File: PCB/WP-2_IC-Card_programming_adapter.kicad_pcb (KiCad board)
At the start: 2 copper layers, 17.8 x 49.5 mm, 4 parts, among them J1 Conn_01x38_Male, J2 Conn_02x16_Counter_Clockwise, J3 Conn_02x08_Odd_Even

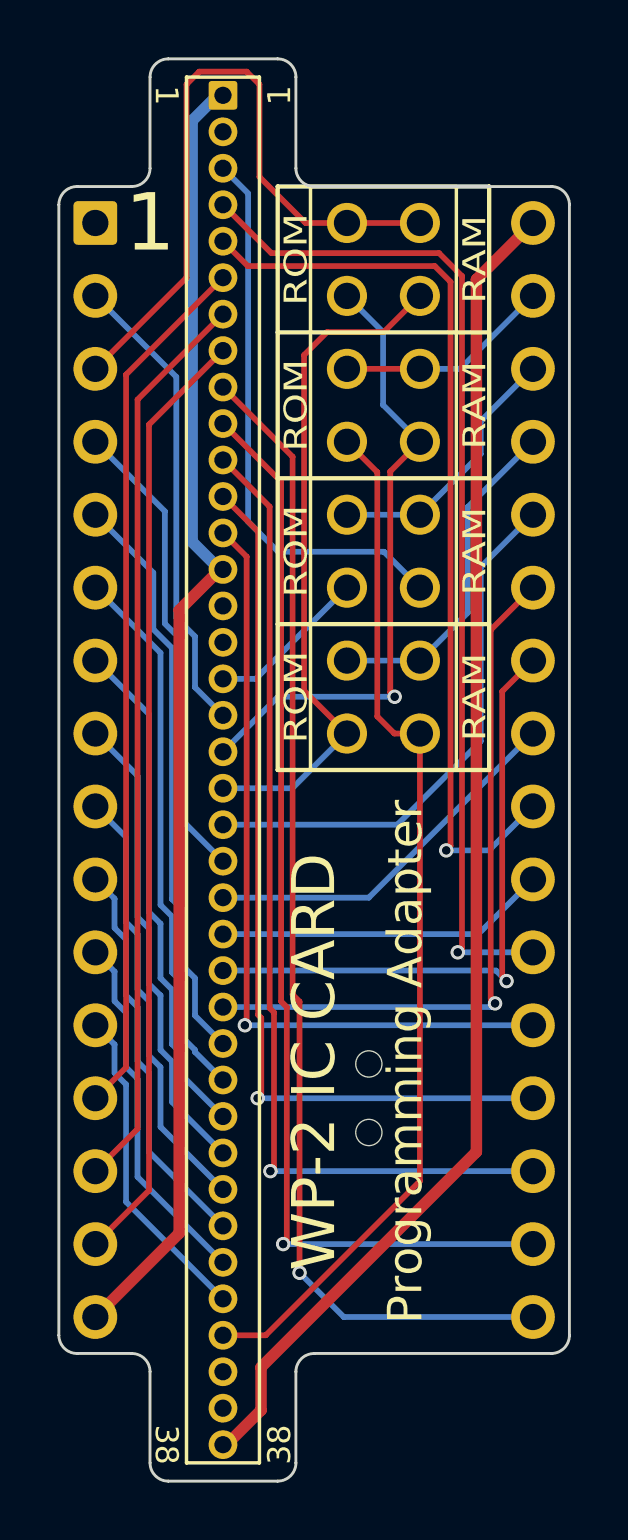
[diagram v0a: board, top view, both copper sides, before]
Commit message: MRAM level shifters, delete FRAM, local datasheets in local symbols
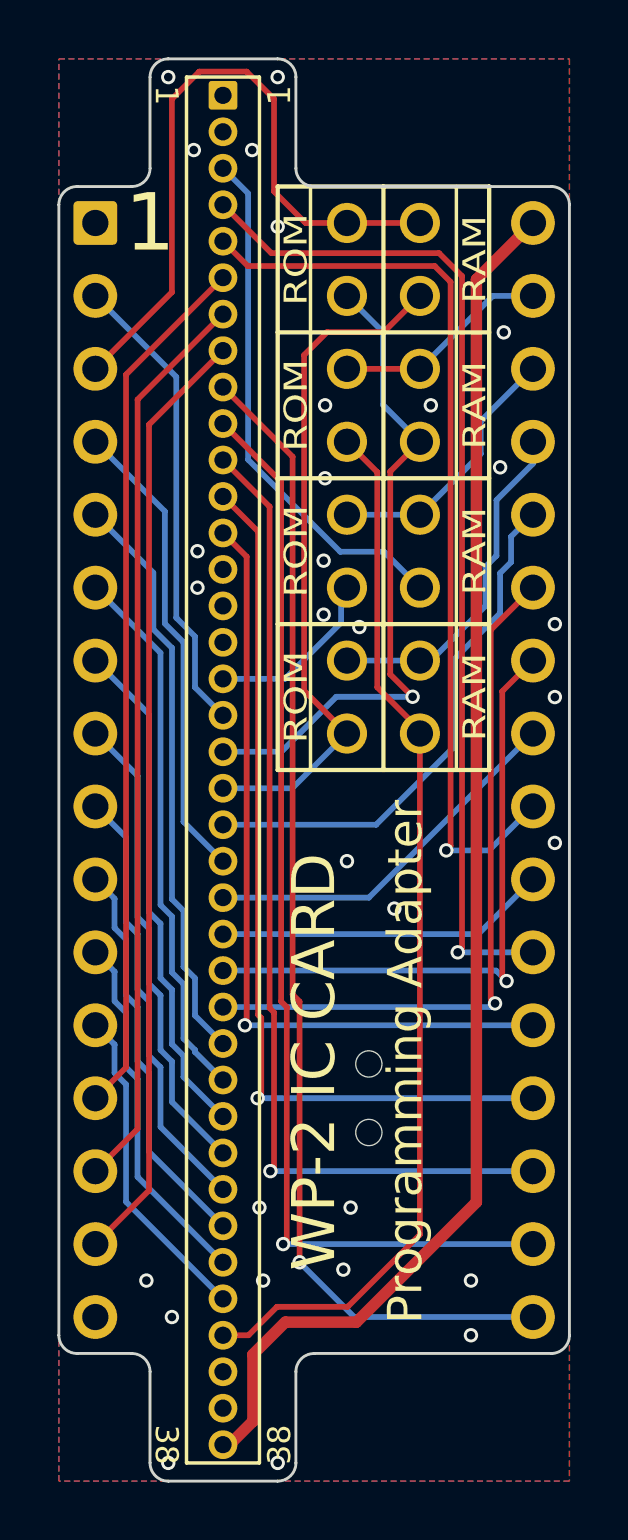
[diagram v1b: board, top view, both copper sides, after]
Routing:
- net GND: track 45.5 -> 0.40 mm, vias 0 -> 30
- net VDD: track 47.1 -> 48.6 mm
- net /CE2: track 19.6 -> 18.3 mm
- net /A15: track 22.3 -> 23.2 mm
- net /A17: track 5.63 -> 6.23 mm
- net /R~{W}: track 36.4 -> 37.0 mm
- added copper zone on B.Cu, net GND
- added copper zone on F.Cu, net GND

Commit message: local symbol & footprint library organization, add shielded mram version
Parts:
- J1: footprint 0_LOCAL:Pin_Header_Straight_1x38_Pitch1.27mm -> 000_LOCAL:Pin_Header_Straight_1x38_Pitch1.27mm
- J2: footprint 0_LOCAL:2x16x600 -> 000_LOCAL:2x16x600
- J3: footprint 0_LOCAL:2x8_jumper_block -> 000_LOCAL:2x8_jumper_block
- REF**: footprint 0_LOCAL:JP2_tight_storage -> 000_LOCAL:JP2_tight_storage

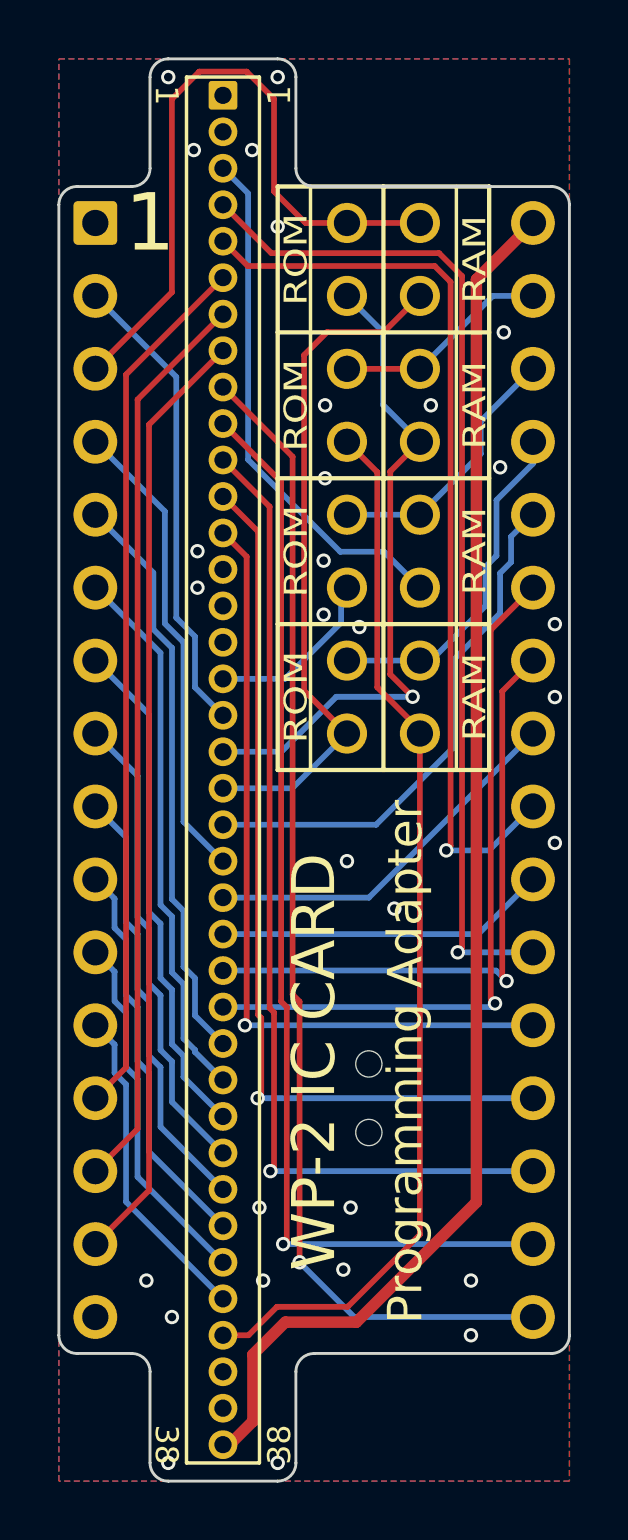
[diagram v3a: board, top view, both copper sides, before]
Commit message: update programming adapter & readme
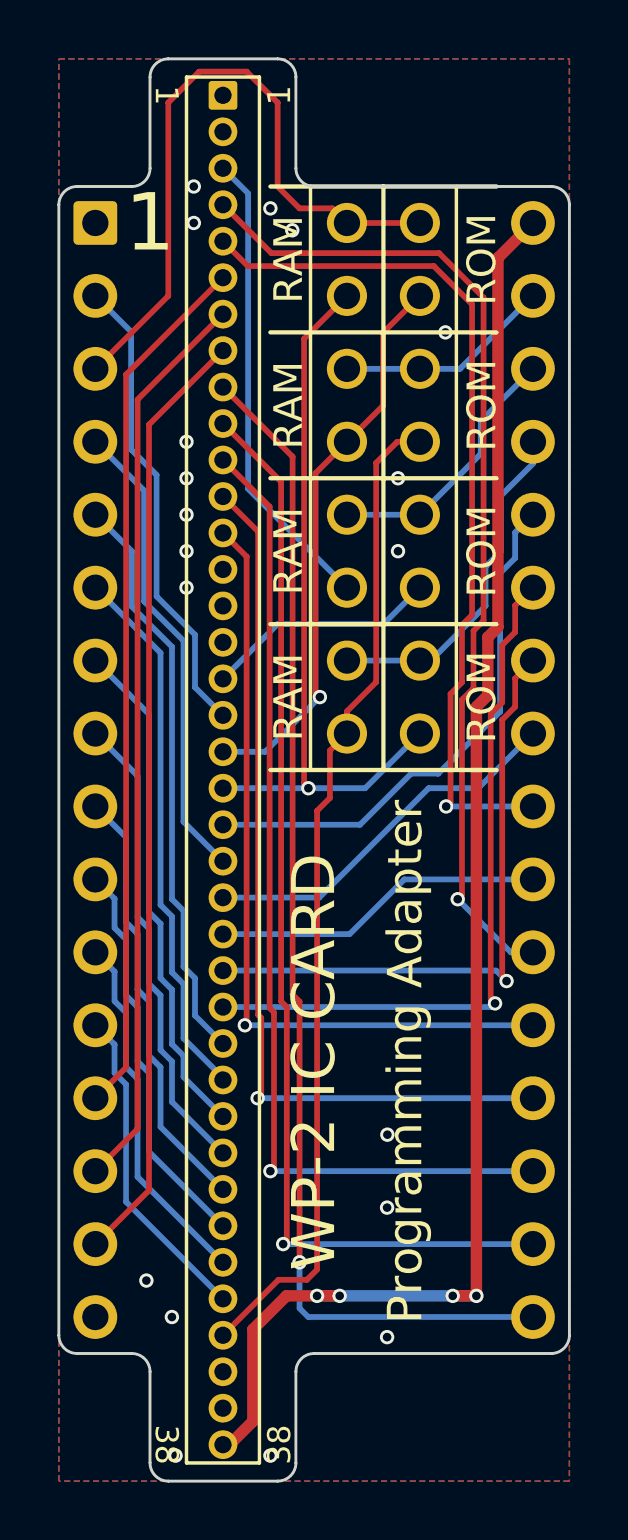
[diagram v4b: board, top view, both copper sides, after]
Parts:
- removed REF**: , 000_LOCAL:JP2_tight_storage
- J2: value Conn_02x16_Counter_Clockwise -> SST39SF020_DIP
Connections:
- net VDD renamed VCC
- J1 pad 14: GND -> /T2
- J1 pad 15: (no net) -> /S1
- J1 pad 16: (no net) -> /S2
- J1 pad 2: (no net) -> /~{DET}
- J1 pad 36: (no net) -> /S3
- J1 pad 37: (no net) -> /BCHK
- J2 pad 1: (no net) -> unconnected-(J2-NC-Pad1)
- J3 pad 11: /A17 -> /CE2
- J3 pad 12: /CE2 -> /A17
- J3 pad 15: /A14 -> /R~{W}
- J3 pad 16: /R~{W} -> /A14
- J3 pad 3: /A15 -> /A14
- J3 pad 4: /A14 -> /A15
- J3 pad 7: /R~{W} -> /A15
- J3 pad 8: /A15 -> /R~{W}
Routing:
- net VCC: track 48.6 -> 52.6 mm, vias 0 -> 4
- net /A15: track 23.2 -> 19.7 mm
- net /R~{W}: track 37.0 -> 35.0 mm
- net /CE2: track 18.3 -> 16.4 mm
- net /A17: track 6.23 -> 8.17 mm
- net /A14: track 23.8 -> 25.5 mm, vias 0 -> 1
- net /~{OE}: track 32.0 -> 30.5 mm
- net /D3: track 40.5 -> 41.4 mm
- net GND: track 0.40 -> 0.19 mm, vias 30 -> 19

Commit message: programming adapter traces away from pads
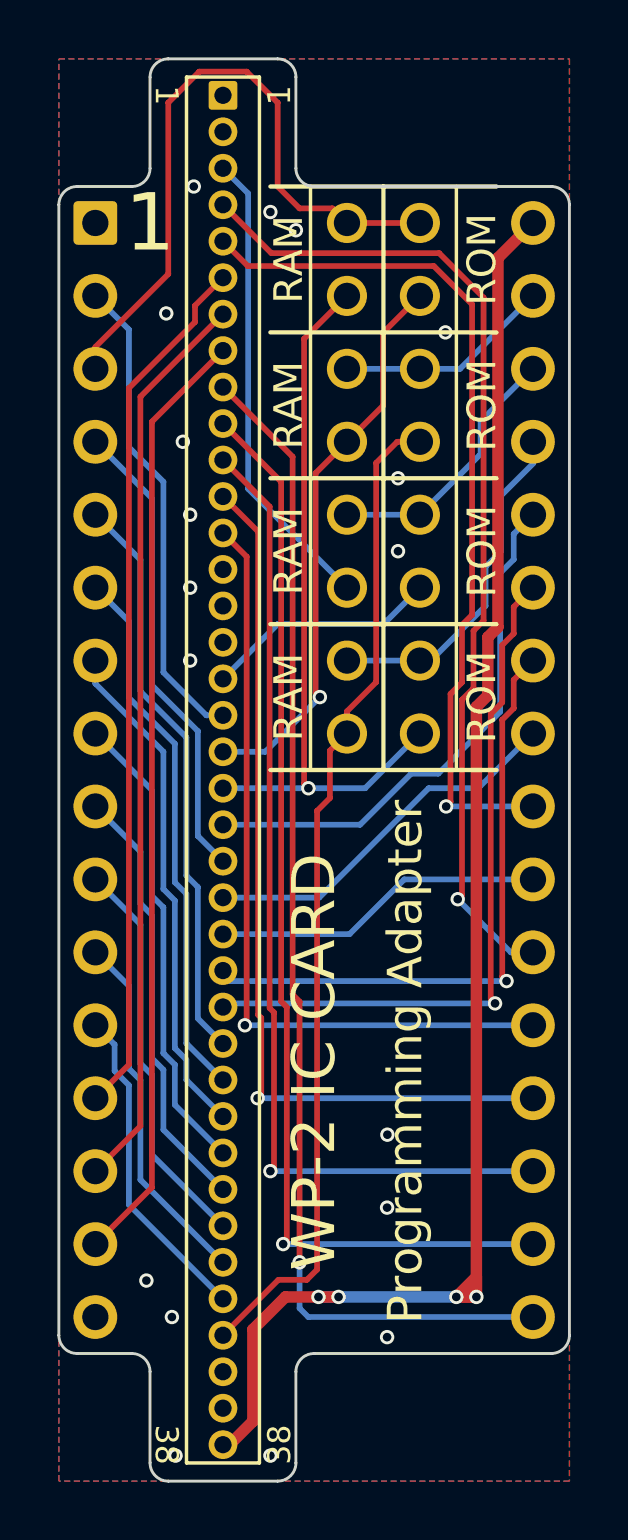
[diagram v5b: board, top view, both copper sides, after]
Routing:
- net GND: vias 19 -> 18
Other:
- board text added: "${TITLE} - ${REVISION}"
- board text removed: "WP-2_IC_Card_programming_adapter v004"

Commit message: add fancy programming adapters, horizontal tray, & full socket
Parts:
- J1: value Conn_01x38_Male -> TMS-138-01; footprint 000_LOCAL:Pin_Header_Straight_1x38_Pitch1.27mm -> 000_LOCAL:TMS-138-01-x-x
